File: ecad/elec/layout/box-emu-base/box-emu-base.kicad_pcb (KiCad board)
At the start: 2 copper layers, 72.5 x 63.9 mm, 69 parts

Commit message: minor update
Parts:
- MECH1, MECH2: value (none) -> SILKSCREENGBC_A/B
- REF**: value (none) -> BOX_EMU_BASE
- U$1: value (none) -> SILKSCREENGBC_D-PAD
- U$2: value (none) -> SILKSCREENGBC_START/SELECT

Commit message: simple layout
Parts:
- moved R17 40.4 mm to (117.4, 128.6)
- moved LED1 36.6 mm to (118.7, 126.9), turned to 180 degrees
- moved R7 8.07 mm to (125.2, 126.8)
- moved C13 3.52 mm to (152.7, 122.9)
- moved C2 1.23 mm to (126.2, 76.3), turned to 90 degrees
- moved C5 0.73 mm to (123.8, 126.0)
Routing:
- net vcc_3v3: track 0.00 -> 161.2 mm, vias 0 -> 11
- net SCL: track 0.00 -> 101.6 mm, vias 0 -> 7
- net vbat: track 5.69 -> 102.6 mm, vias 2 -> 4
- net SDA: track 0.00 -> 96.3 mm, vias 0 -> 5
- net left: track 0.00 -> 96.2 mm, vias 0 -> 4
- net down: track 0.00 -> 87.6 mm, vias 0 -> 6
- net DATA_N: track 0.00 -> 67.4 mm, vias 0 -> 3
- net line: track 0.00 -> 64.9 mm, vias 0 -> 4
- net DATA_P: track 0.00 -> 63.8 mm, vias 0 -> 2
- net vcc_5v: track 4.04 -> 67.6 mm, vias 0 -> 4
- net vol_up: track 0.00 -> 56.1 mm, vias 0 -> 6
- net cs-2: track 0.00 -> 55.2 mm, vias 0 -> 2
- net MOSI: track 0.00 -> 53.7 mm, vias 0 -> 2
- net SCLK: track 0.00 -> 52.4 mm, vias 0 -> 2
- net up: track 0.00 -> 52.3 mm, vias 0 -> 4
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- added copper zone on B.Cu, net gnd

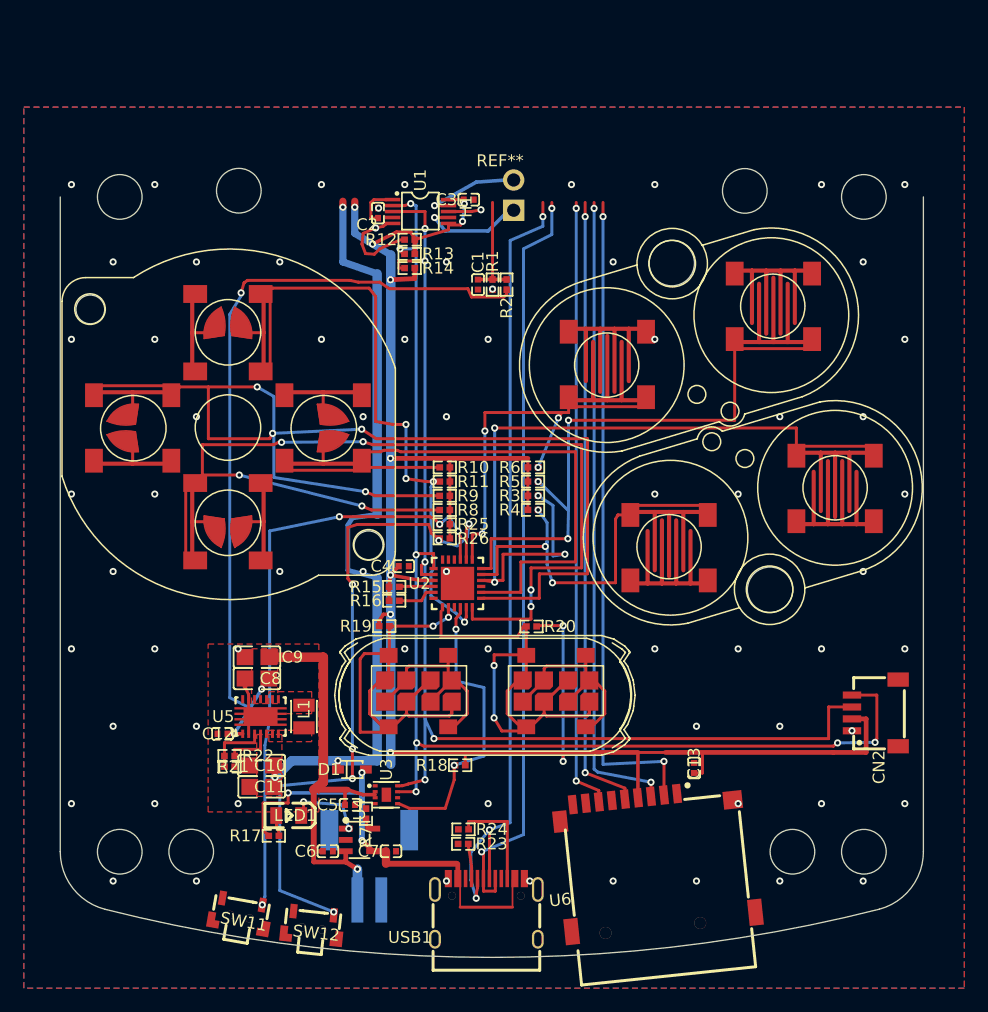
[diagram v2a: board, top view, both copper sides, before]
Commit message: update to work with latest atopile services (lack thereof)
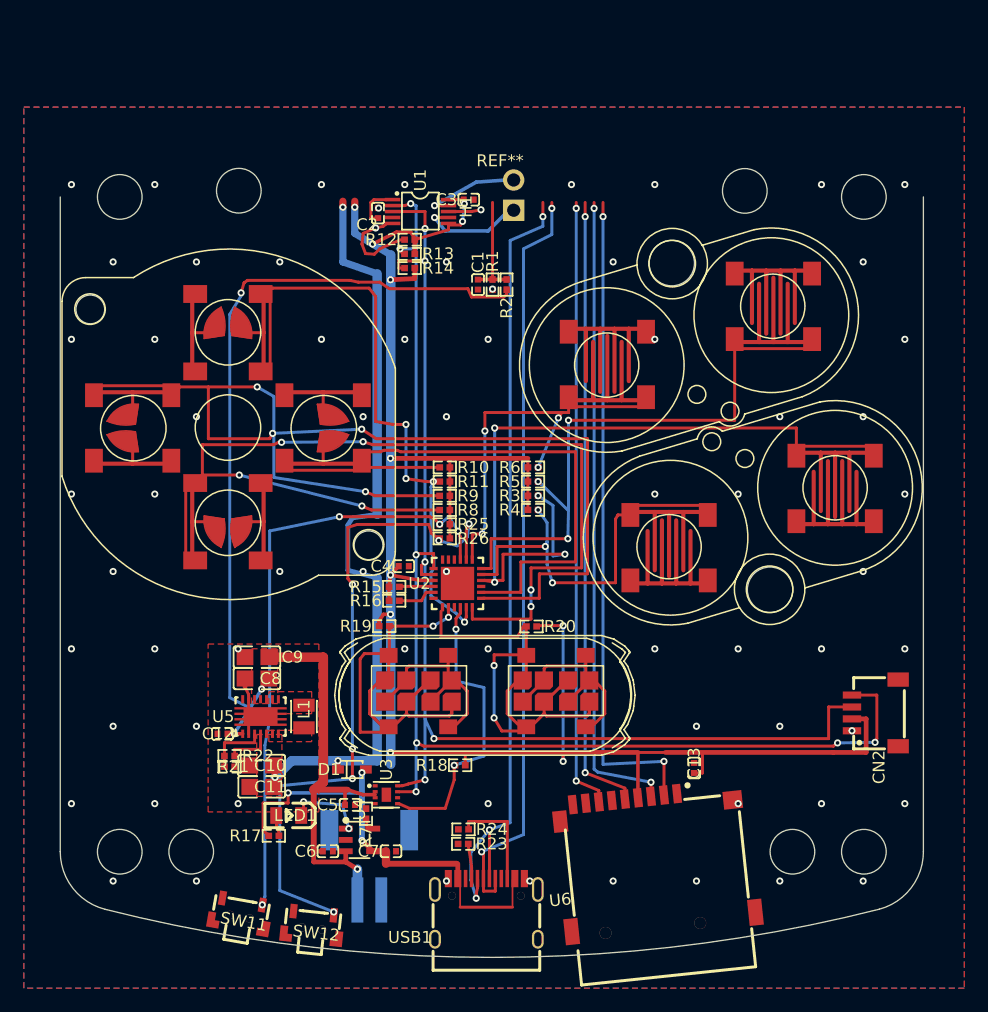
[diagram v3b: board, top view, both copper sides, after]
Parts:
- C12: value 100nF ±10% -> 100nF ±20%
- C2: value 1µF ±10% -> 1µF ±20%
- C8, C9: value 10µF ±10% -> 10µF ±20%
- MECH1, MECH2: value SILKSCREENGBC_A/B -> (none)
- R10, R11, R12, R13, R14, R15, R16, R18, R19, R20, R25, R26, R3, R4, R5, R6, R8, R9: value 10kΩ ±1% -> 10kΩ ±5%
- R17, R23, R24: value 5.1kΩ ±1% -> 5.1kΩ ±5%
- R7: value 2kΩ ±1% -> 2kΩ ±5%
- REF**: value BOX_EMU_BASE -> (none)
- U$1: value SILKSCREENGBC_D-PAD -> (none)
- U$2: value SILKSCREENGBC_START/SELECT -> (none)

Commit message: update routing
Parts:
- MECH1, MECH2: value (none) -> SILKSCREENGBC_A/B
- REF**: value (none) -> BOX_EMU_BASE
- U$1: value (none) -> SILKSCREENGBC_D-PAD
- U$2: value (none) -> SILKSCREENGBC_START/SELECT
- moved R9 22.0 mm to (111.1, 92.6), turned to 0 degrees
- moved R8 19.2 mm to (112.9, 97.8), turned to -90 degrees
- moved R11 17.2 mm to (119.1, 110.5), turned to 0 degrees
- moved R10 12.0 mm to (119.8, 98.6), turned to 90 degrees
- moved R3 9.59 mm to (138.0, 109.6), turned to 90 degrees
- moved R6 7.02 mm to (135.4, 103.6), turned to -90 degrees
- moved R5 5.63 mm to (138.0, 104.4), turned to -90 degrees
- moved R4 5.18 mm to (138.9, 106.4), turned to -90 degrees
- moved R26 1.83 mm to (133.6, 103.9), turned to -90 degrees
- moved R25 1.32 mm to (132.8, 103.3), turned to -90 degrees
- moved R19 0.97 mm to (127.1, 110.1), turned to -90 degrees
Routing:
- net vcc_3v3: track 161.2 -> 237.9 mm, vias 11 -> 18
- net down: track 87.6 -> 46.2 mm, vias 6 -> 2
- net left: track 96.2 -> 68.9 mm, vias 4 -> 2
- net line: track 64.9 -> 46.8 mm, vias 4 -> 0
- net select: track 17.9 -> 35.6 mm
- net up: track 52.3 -> 67.6 mm, vias 4 -> 2
- net b-line: track 34.1 -> 24.1 mm, vias 3 -> 0
- net right: track 51.7 -> 41.9 mm, vias 0 -> 2
- net vol_up: track 56.1 -> 50.9 mm
- net x_y_btns-b-line: track 34.1 -> 29.0 mm, vias 4 -> 2
- net x_y_btns-a-line: track 51.4 -> 47.6 mm, vias 3 -> 0
- net start: track 22.0 -> 23.4 mm, vias 2 -> 4
- net gnd: track 5.80 -> 6.65 mm, vias 67 -> 70
- net vol_down: track 50.7 -> 50.1 mm, vias 4 -> 3
